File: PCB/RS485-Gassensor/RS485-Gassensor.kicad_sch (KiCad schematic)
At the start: 54 parts, among them J1 Screw_Terminal_01x08, J2 Screw_Terminal_01x04, J3 Screw_Terminal_01x08, J4 Screw_Terminal_01x06, J5 Screw_Terminal_01x06, SW1 SW_DIP_x06, U1 STM32G031K8Tx, U2 STM32G031K8Ux, U3 MQ-6, U4 OKI-78SR-5_1.5-W36-C, U5 AP2127N-3.3, U6 AD8676xR, U7 LT1785xS8, U8 MQ-6, U9 AD8676xR

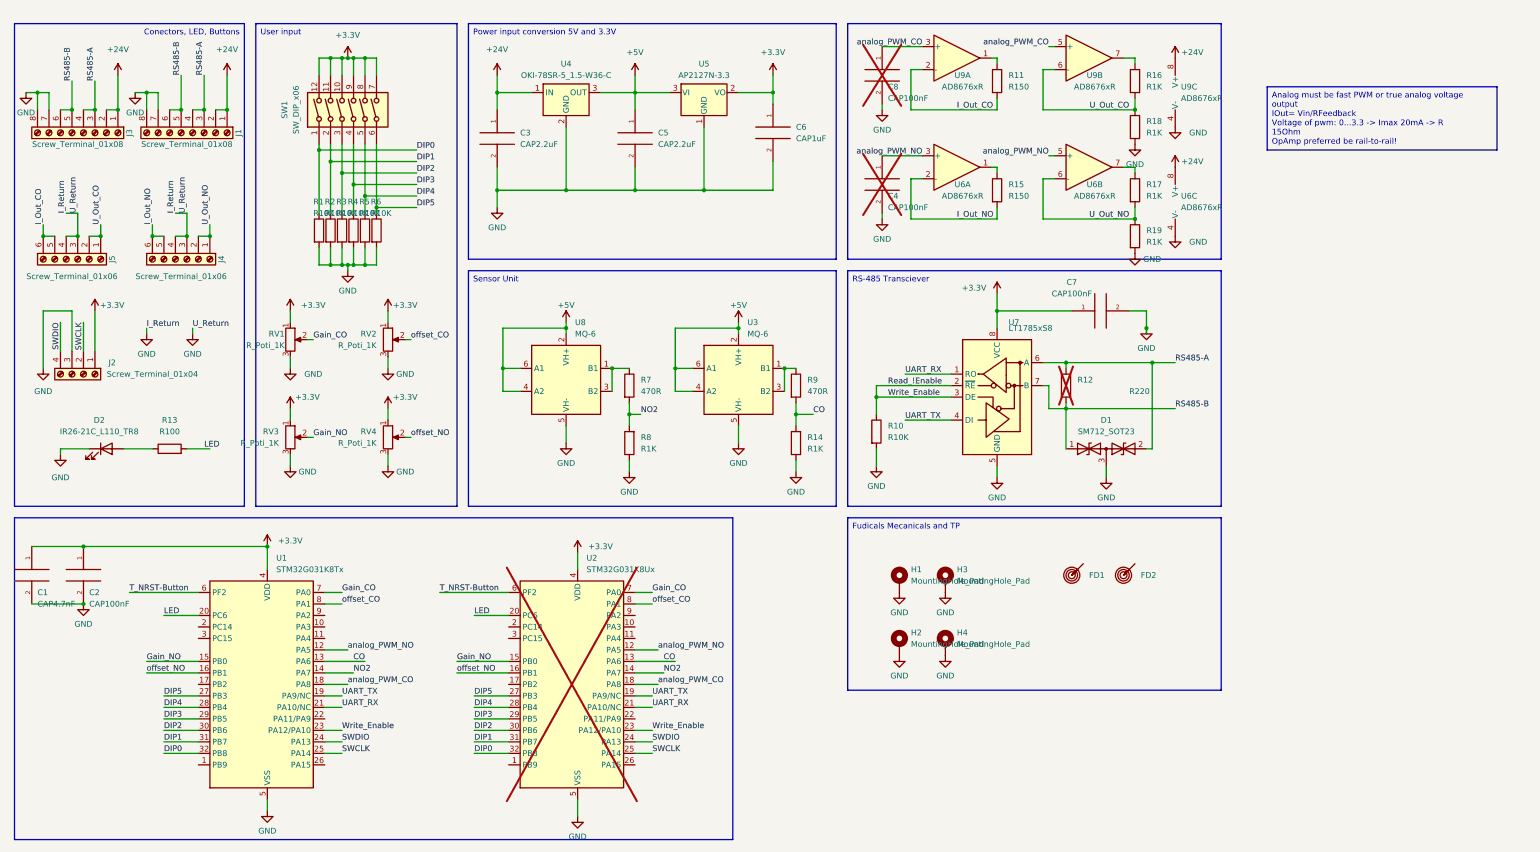
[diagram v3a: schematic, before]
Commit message: imoproved filter
one dual channel Op amp, corrections from first produced prototype
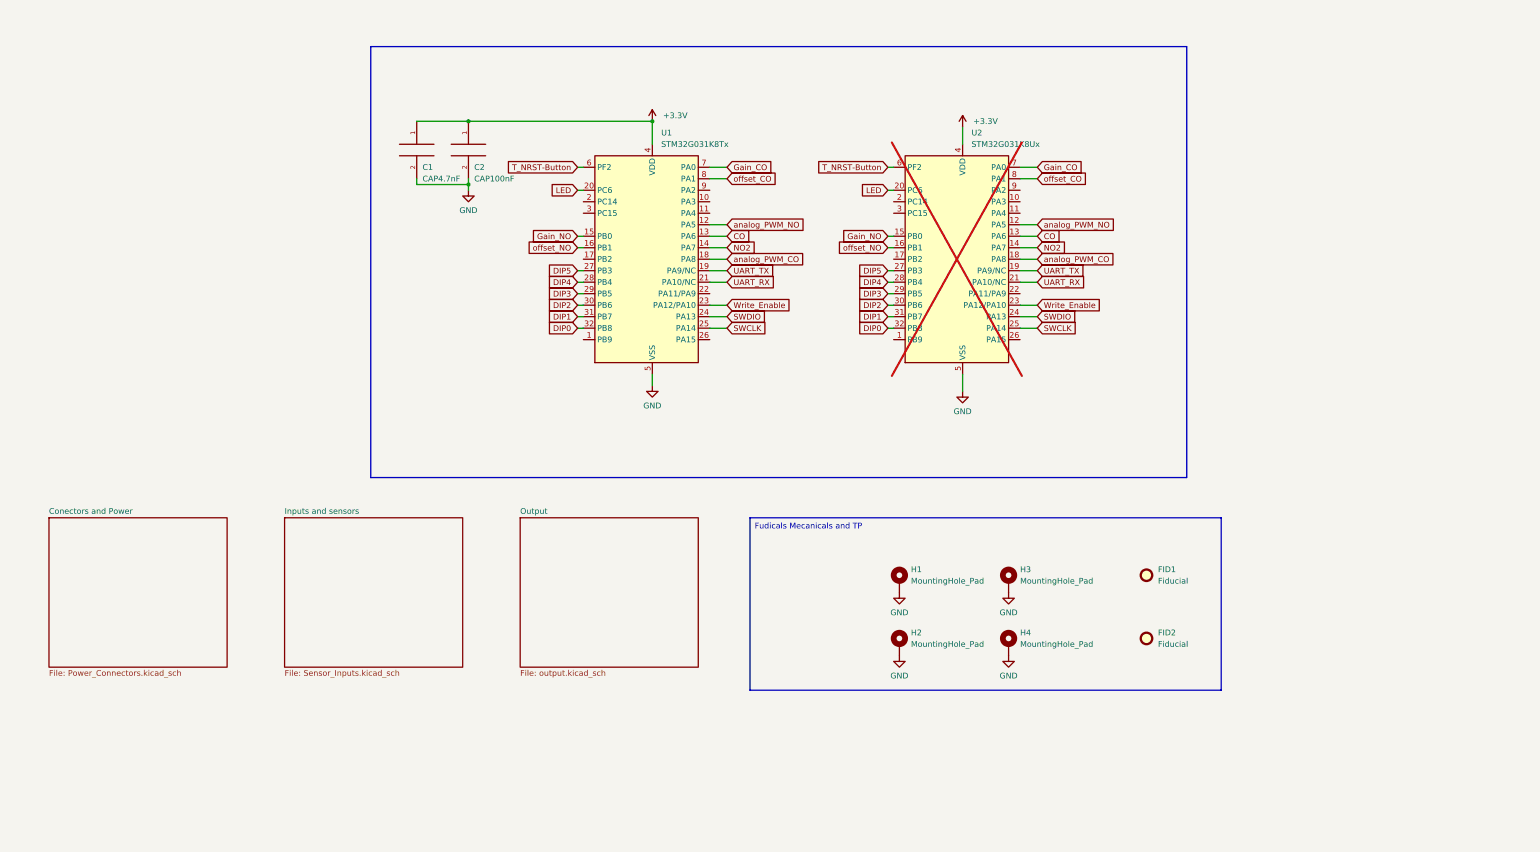
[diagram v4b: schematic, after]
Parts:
- removed C3, C5: CAP2.2uF, Capacitor_SMD:C_0603_1608Metric, symbol pspice:CAP
- removed C4, C7, C8: CAP100nF, Capacitor_SMD:C_0603_1608Metric, symbol pspice:CAP
- removed C6: CAP1uF, Capacitor_SMD:C_0603_1608Metric, symbol pspice:CAP
- removed D1: SM712_SOT23, Package_TO_SOT_SMD:SOT-23, symbol Diode:SM712_SOT23
- removed D2: IR26-21C_L110_TR8, LED_SMD:LED_1206_3216Metric, symbol LED:IR26-21C_L110_TR8
- removed FD1, FD2: ~, Custom_Library:Alignement_Testpoint_2Layer, symbol Custom:Alignement_Testpoint
- removed J1, J3: Screw_Terminal_01x08, Connector_Phoenix_SPT:1862068, symbol Connector:Screw_Terminal_01x08
- removed J2: Screw_Terminal_01x04, Connector_PinHeader_2.54mm:PinHeader_1x04_P2.54mm_Vertical, symbol Connector:Screw_Terminal_01x04
- removed J4, J5: Screw_Terminal_01x06, Connector_Phoenix_SPT:1071000, symbol Connector:Screw_Terminal_01x06
- removed R1, R10, R2, R3, R4, R5, R6: R10K, Capacitor_SMD:C_0603_1608Metric, symbol Device:R
- removed R11, R15: R150, Capacitor_SMD:C_1206_3216Metric, symbol Device:R
- removed R12: R220, Capacitor_SMD:C_0603_1608Metric, symbol Device:R
- removed R13: R100, Capacitor_SMD:C_0603_1608Metric, symbol Device:R
- removed R14, R16, R17, R18, R19, R8: R1K, Capacitor_SMD:C_0603_1608Metric, symbol Device:R
- removed R7, R9: 470R, Capacitor_SMD:C_0603_1608Metric, symbol Device:R
- removed RV1, RV2, RV3, RV4: R_Poti_1K, PCM_Potentiometer_SMD_AKL:Potentiometer_Bourns_3214J_Horizontal, symbol Device:R_Potentiometer
- removed SW1: SW_DIP_x06, Package_DIP:SMDIP-12_W9.53mm, symbol Switch:SW_DIP_x06
- removed U3, U8: MQ-6, Sensor:MQ-6, symbol Sensor_Gas:MQ-6
- removed U4: OKI-78SR-5_1.5-W36-C, Converter_DCDC:Converter_DCDC_Murata_OKI-78SR_Vertical, symbol Converter_DCDC:OKI-78SR-5_1.5-W36-C
- removed U5: AP2127N-3.3, Package_TO_SOT_SMD:SOT-23, symbol Regulator_Linear:AP2127N-3.3
- removed U6, U9: AD8676xR, Package_SO:SOIC-8_3.9x4.9mm_P1.27mm, symbol Amplifier_Operational:AD8676xR
- removed U7: LT1785xS8, PCM_Package_SO_AKL:SOIC-8_3.9x4.9mm_P1.27mm, symbol Interface_UART:LT1785xS8
- added FID1, FID2: Fiducial, Fiducial:Fiducial_1.5mm_Mask3mm, symbol Mechanical:Fiducial
- C1, C2: footprint Capacitor_SMD:C_0603_1608Metric -> Capacitor_SMD:C_1206_3216Metric
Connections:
- net Read_!Enable renamed Write_Enable
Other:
- added sheet Conectors and Power (Power_Connectors.kicad_sch)
- added sheet Inputs and sensors (Sensor_Inputs.kicad_sch)
- added sheet Output (output.kicad_sch)
- title: (none) -> NO-CO Gas sensor
- moved on the sheet: C1, C2, H3, H4, U1, U2

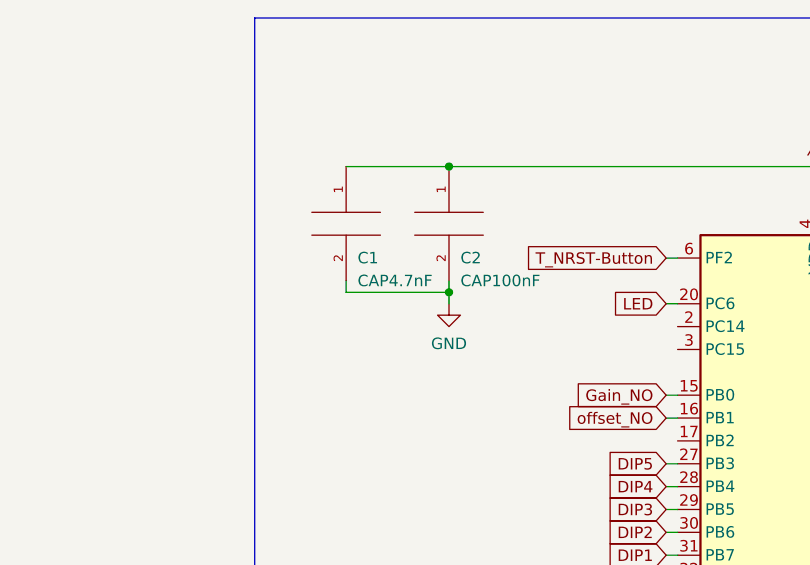
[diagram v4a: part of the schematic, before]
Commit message: added Modbus / RS485
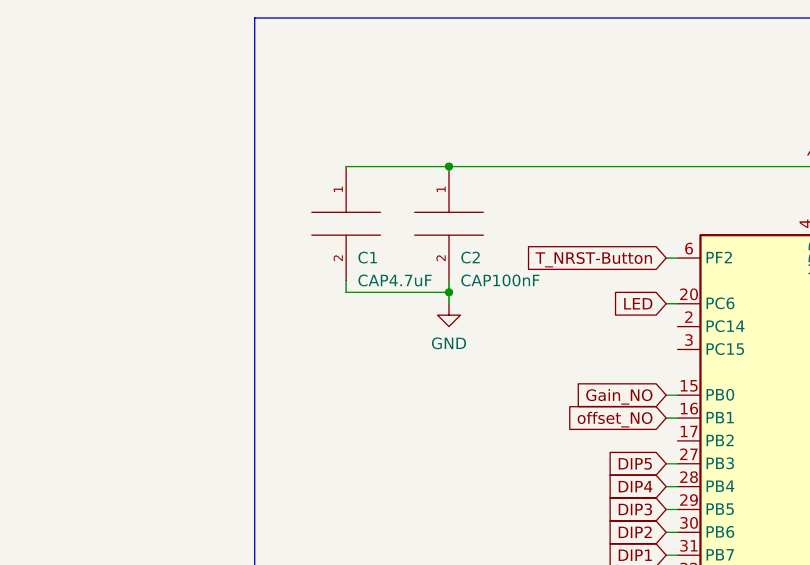
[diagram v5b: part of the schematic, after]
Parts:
- C1: value CAP4.7nF -> CAP4.7uF
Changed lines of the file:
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@@
       (effects (font (size 1.27 1.27)) (justify left))
     )
-    (property "Value" "CAP4.7nF" (at 105.41 50.8 0)
+    (property "Value" "CAP4.7uF" (at 105.41 50.8 0)
       (effects (font (size 1.27 1.27)) (justify left))
     )

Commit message: made For NAP505 and NAP550
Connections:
- net DIP0: now also U1.2 (PC14), U2.2 (PC14); no longer U1.32 (PB8), U2.32 (PB8)
- net DIP1: now also U1.32 (PB8), U2.32 (PB8); no longer U1.31 (PB7), U2.31 (PB7)
- net DIP2: now also U1.31 (PB7), U2.31 (PB7); no longer U1.30 (PB6), U2.30 (PB6)
- net I2C_SDA: now reaches U2.1 (PB9)
- net I2C_SDA: now also U1.1 (PB9)
- new net I2C_SCL: U1.30 (PB6), U2.30 (PB6)
